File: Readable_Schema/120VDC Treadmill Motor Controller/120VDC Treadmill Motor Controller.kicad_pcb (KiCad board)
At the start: 2 copper layers, 171.2 x 90.5 mm, 75 parts, among them J1 TB005-762-03BE, J2 OSTT7020150, J3 TB0011-350-08BE, J4 TB0011-350-08BE, J5 TB0011-350-08BE, J6 TB0011-350-03BE, J7 TB005-762-02BE, K1 T9GV1L14-24, Q1 IPP200N25N3GXKSA1, Q2 IPP200N25N3GXKSA1, Q4 IPP200N25N3GXKSA1, Q5 MUN5330DW1, Q6 MUN5330DW1T1G, Q7 IPP200N25N3GXKSA1, Q8 SMUN5230DW1T1G, Q9 IPP200N25N3GXKSA1, U1 FOD3182, U10 FOD3182, U11 TC75S56F_LF, U2 FOD3182, U3 TMCS1126B42QDVGRQ1, U4 FOD3182, U5 NLV14044BDR2G, U6 NC7SZ04P5X, U7 FOD3182, U8 RAC05E-05SKT, U9 SN74LVC1G08DCKR

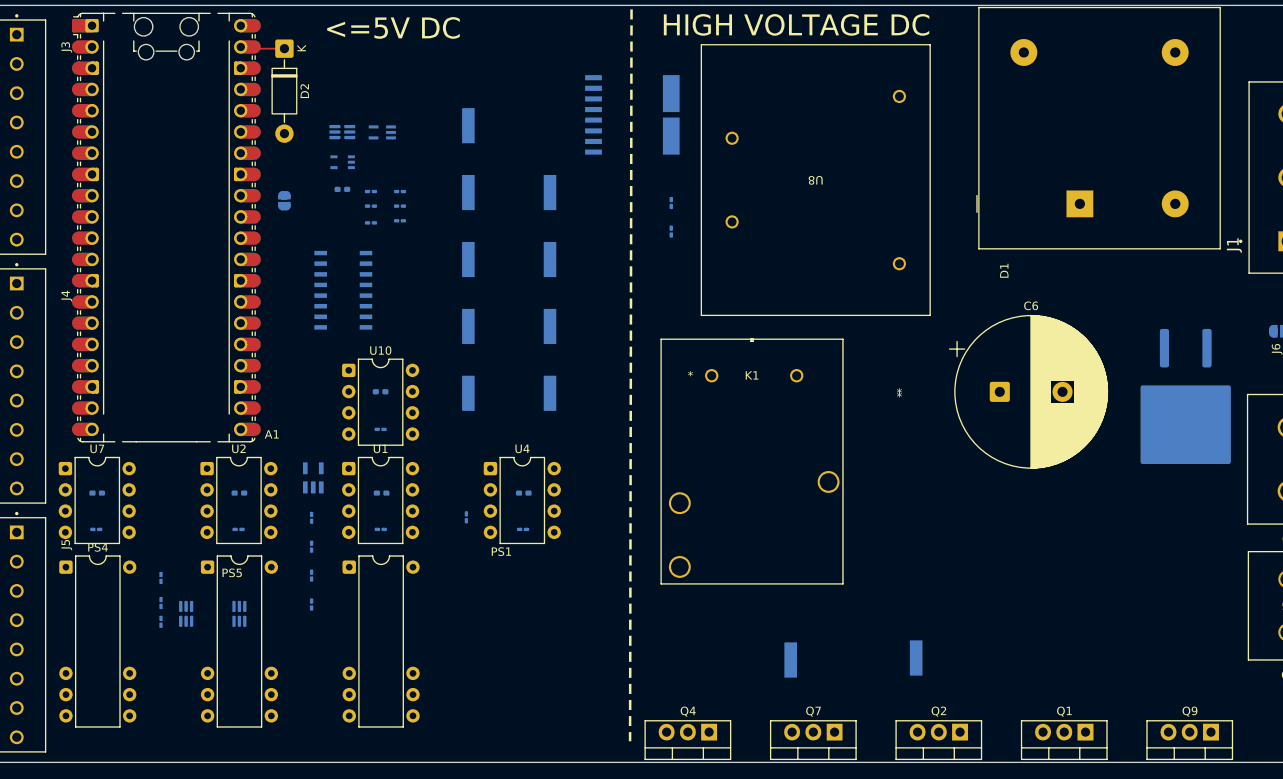
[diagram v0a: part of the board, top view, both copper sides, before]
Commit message: Finished choosing real components for the digitally isolated drives. Mainly followed TIs 100khz example and chose to use mostly repeat components. Now confirming the design doesnt suck then working on traces
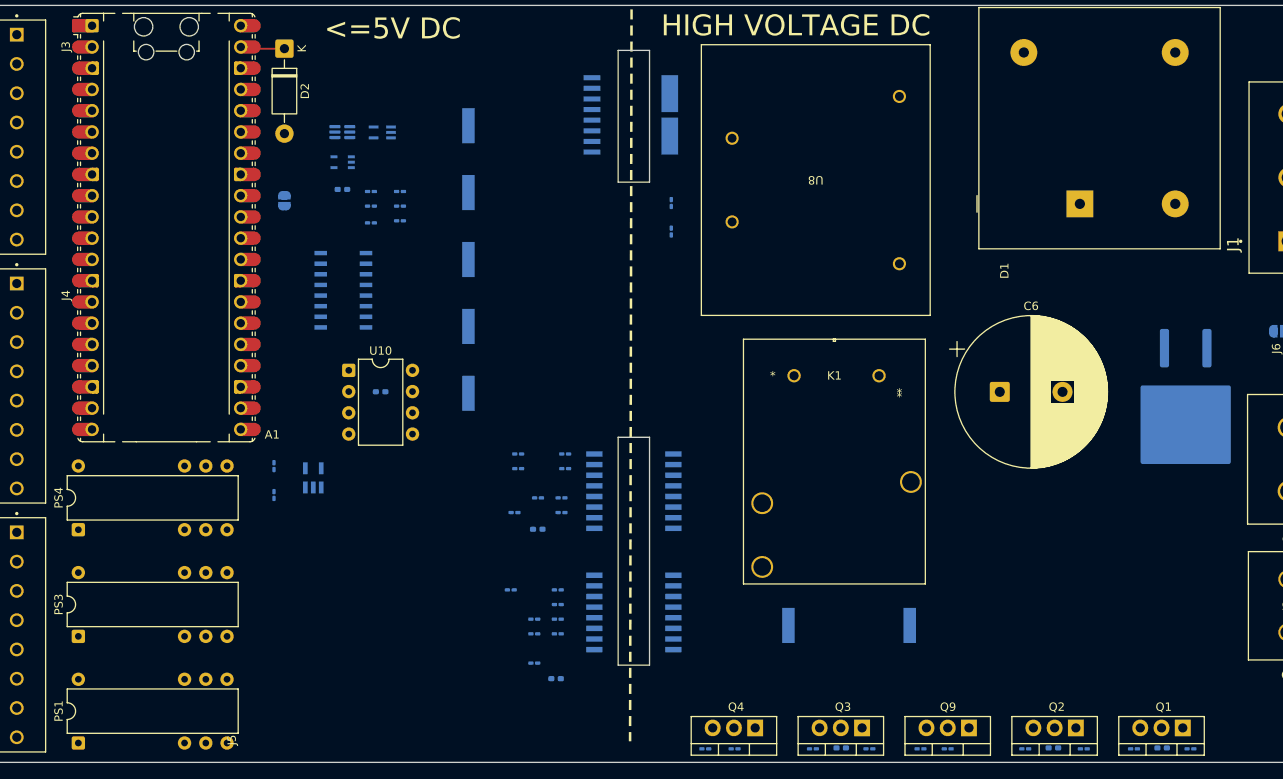
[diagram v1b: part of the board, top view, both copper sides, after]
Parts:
- removed PS5: SRS-0515-2, Footprints_TMC:SRS-0515 DIP-16_W7.62mm
- removed Q6: MUN5330DW1T1G, Package_TO_SOT_SMD:SOT-363_SC-70-6
- removed Q7: IPP200N25N3GXKSA1, Package_TO_SOT_THT:TO-220-3_Vertical
- removed Q8: SMUN5230DW1T1G, Package_TO_SOT_SMD:SOT-363_SC-70-6
- removed TP3, TP4, TP5, TP6: RCWCTE, Treadmill_Feet:RCWCTE
- removed U4, U7: FOD3182, Package_DIP:DIP-8_W7.62mm
- added C10: 0.1u, Capacitor_SMD:C_0402_1005Metric_Pad0.74x0.62mm_HandSolder, B.Cu at (213.2, 148.4)
- added C11: 0.1u, Capacitor_SMD:C_0402_1005Metric_Pad0.74x0.62mm_HandSolder, B.Cu at (200.2, 148.4)
- added C12: 0.1u, Capacitor_SMD:C_0402_1005Metric_Pad0.74x0.62mm_HandSolder, B.Cu at (174.8, 148.4)
- added C13: 33pF, Capacitor_SMD:C_0201_0603Metric_Pad0.64x0.40mm_HandSolder, B.Cu at (141.4, 120.2)
- added C14: 33pF, Capacitor_SMD:C_0201_0603Metric_Pad0.64x0.40mm_HandSolder, B.Cu at (141.8, 113.2)
- added C15: 33pF, Capacitor_SMD:C_0201_0603Metric_Pad0.64x0.40mm_HandSolder, B.Cu at (141.8, 115.0)
- added C16: 0.1u, Capacitor_SMD:C_0402_1005Metric_Pad0.74x0.62mm_HandSolder, B.Cu at (138.5, 122.2)
- added C8: 33pF, Capacitor_SMD:C_0201_0603Metric_Pad0.64x0.40mm_HandSolder, B.Cu at (140.9, 134.8)
- added C9: 33pF, Capacitor_SMD:C_0201_0603Metric_Pad0.64x0.40mm_HandSolder, B.Cu at (141.4, 118.5)
- added PS3: SRS-0515-2, Footprints_TMC:SRS-0515 DIP-16_W7.62mm, F.Cu at (83.6, 135.1)
- added Q3: IPP200N25N3GXKSA1, Package_TO_SOT_THT:TO-220-3_Vertical, F.Cu at (177.3, 146.0)
- added R18: 10K, Resistor_SMD:R_0201_0603Metric_Pad0.64x0.40mm_HandSolder, B.Cu at (136.2, 113.2)
- added R23: 10K, Resistor_SMD:R_0201_0603Metric_Pad0.64x0.40mm_HandSolder, B.Cu at (136.2, 115.0)
- added R24: 10, Resistor_SMD:R_0201_0603Metric_Pad0.64x0.40mm_HandSolder, B.Cu at (209.8, 148.5)
- added R25: 10, Resistor_SMD:R_0201_0603Metric_Pad0.64x0.40mm_HandSolder, B.Cu at (158.6, 148.5)
- added R26: 10K, Resistor_SMD:R_0201_0603Metric_Pad0.64x0.40mm_HandSolder, B.Cu at (216.6, 148.5)
- added R27: 10K, Resistor_SMD:R_0201_0603Metric_Pad0.64x0.40mm_HandSolder, B.Cu at (162.1, 148.5)
- added R28: 10K, Resistor_SMD:R_0201_0603Metric_Pad0.64x0.40mm_HandSolder, B.Cu at (187.5, 148.5)
- C1, C2, C3: value 0.1u -> 33pF; footprint Capacitor_SMD:C_0402_1005Metric_Pad0.74x0.62mm_HandSolder -> Capacitor_SMD:C_0201_0603Metric_Pad0.64x0.40mm_HandSolder
- R1, R2: value 10 -> 50
- R10, R5: value 100 -> 10K
- R15, R6: value 10 -> 10K
- R16, R4: value 100 -> 50
- R7, R8: value 100 -> 10
- U1, U2: value FOD3182 -> UCC21530DWKR; footprint Package_DIP:DIP-8_W7.62mm -> Treadmill_Feet:SOIC127P1030X265-16N; moved to B.Cu
- moved R7 105.3 mm to (196.8, 148.5), turned to 0 degrees
- moved R15 96.1 mm to (178.2, 148.5), turned to 0 degrees
- moved R10 95.4 mm to (203.8, 148.5), turned to 0 degrees
- moved R8 79.9 mm to (171.4, 148.5), turned to 0 degrees
- moved R12 75.0 mm to (184.3, 148.5), turned to 0 degrees
- moved C5 59.2 mm to (140.7, 140.1)
- moved U2 53.8 mm to (150.0, 132.2)
- moved R5 44.9 mm to (138.1, 138.2), turned to 180 degrees
- moved C2 40.3 mm to (140.9, 131.2)
- moved PS1 38.6 mm to (83.6, 147.8), turned to 90 degrees
- moved R2 37.5 mm to (138.1, 134.8)
- moved U1 34.2 mm to (150.0, 117.7)
- moved Q9 28.9 mm to (190.1, 146.0)
- moved R4 27.2 mm to (138.6, 118.5), turned to 180 degrees
- moved C1 24.0 mm to (140.9, 129.5)
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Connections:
- A1 pad 27: /H_Bridge/dir -> /Pi Pico/dir_mcu
- C1 pad 1: GND1 -> Net-(U2-INB)
- C1 pad 2: /Brake_Resistor/ps_in_+ -> GND
- C2 pad 1: /H_Bridge/Fet Circuit1/lg -> Net-(U2-DT)
- C2 pad 2: Net-(U2-VCC) -> GND
- C3 pad 1: GND1 -> Net-(U2-INA)
- C3 pad 2: /Brake_Resistor/ps_in_+ -> GND
- C5 pad 1: /H_Bridge/Fet Circuit/lg -> 5v 5w
- C5 pad 2: Net-(U7-VCC) -> GND
- J2 pad 1: /H_Bridge/Fet Circuit/lg -> /H_Bridge/hs_ps_1_-
- J2 pad 2: /H_Bridge/Fet Circuit1/lg -> /H_Bridge/hs_ps_2_-
- PS1 pad 7: /Brake_Resistor/ps_in_+ -> /H_Bridge/ls_ps_+
- PS4 pad 11: /H_Bridge/Fet Circuit/lg -> /H_Bridge/hs_ps_2_-
- PS4 pad 7: Net-(U7-VCC) -> /H_Bridge/hs_ps_2_+
- Q1 pad 1: /H_Bridge/Fet Circuit/lg -> /Feedback/in-
- Q1 pad 3: GND1 -> /H_Bridge/hs_ps_2_-
- Q2 pad 3: /H_Bridge/Fet Circuit1/lg -> /H_Bridge/hs_ps_1_-
- Q4 pad 1: /H_Bridge/Fet Circuit1/lg -> /H_Bridge/hs_ps_2_-
- R1 pad 1: Net-(R1-Pad1) -> /H_Bridge/dir_b
- R1 pad 2: Net-(Q1-G) -> Net-(U2-INB)
- R10 pad 1: 3v3 MCU -> /H_Bridge/hs_ps_1_-
- R10 pad 2: Net-(Q8B-C2) -> Net-(Q2-G)
- R15 pad 1: Net-(R15-Pad1) -> GND1
- R15 pad 2: Net-(Q7-G) -> Net-(Q3-G)
- R16 pad 1: /H_Bridge/LS FET/v_pwm -> /H_Bridge/dir_a
- R16 pad 2: /H_Bridge/dir -> Net-(U1-INB)
- R2 pad 1: Net-(R2-Pad1) -> /H_Bridge/pwm_a
- R2 pad 2: Net-(Q2-G) -> Net-(U2-INA)
- R4 pad 1: Net-(Q8B-C2) -> /H_Bridge/pwm_b
- R4 pad 2: /H_Bridge/LS FET1/v_pwm -> Net-(U1-INA)
- R5 pad 1: Net-(Q6B-C2) -> Net-(U2-EN)
- R5 pad 2: /H_Bridge/Fet Circuit/v_pwm -> Net-(U2-VCCI_2)
- R6 pad 1: Net-(R6-Pad1) -> Net-(U2-DT)
- R6 pad 2: Net-(Q4-G) -> GND
- R7 pad 1: /H_Bridge/Fet Circuit1/v_pwm -> Net-(U2-OUTA)
- R7 pad 2: Net-(Q8A-C1) -> Net-(Q2-G)
- R8 pad 1: Net-(Q8A-C1) -> Net-(U2-OUTB)
- R8 pad 2: /Feedback/pwm -> Net-(Q3-G)
- TP1 pad 1: /H_Bridge/Fet Circuit/lg -> /H_Bridge/hs_ps_1_-
- TP2 pad 1: /H_Bridge/Fet Circuit1/lg -> /H_Bridge/hs_ps_2_-
- U1 pad 1: unconnected-(U1-NC-Pad1) -> Net-(U1-INA)
- U1 pad 2: GND1 -> Net-(U1-INB)
- U1 pad 3: /H_Bridge/LS FET1/v_pwm -> 5v 5w
- U1 pad 4: unconnected-(U1-NC-Pad4) -> GND
- U1 pad 5: GND1 -> Net-(U1-EN)
- U1 pad 6: Net-(R1-Pad1) -> Net-(U1-DT)
- U1 pad 7: Net-(R1-Pad1) -> unconnected-(U1-NC-Pad7)
- U1 pad 8: /Brake_Resistor/ps_in_+ -> Net-(U1-VCCI_2)
- U2 pad 1: unconnected-(U2-NC-Pad1) -> Net-(U2-INA)
- U2 pad 2: GND -> Net-(U2-INB)
- U2 pad 3: /H_Bridge/Fet Circuit1/v_pwm -> 5v 5w
- U2 pad 4: unconnected-(U2-NC-Pad4) -> GND
- U2 pad 5: /H_Bridge/Fet Circuit1/lg -> Net-(U2-EN)
- U2 pad 6: Net-(R2-Pad1) -> Net-(U2-DT)
- U2 pad 7: Net-(R2-Pad1) -> unconnected-(U2-NC-Pad7)
- U2 pad 8: Net-(U2-VCC) -> Net-(U2-VCCI_2)
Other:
- outline, holes or cut-outs redrawn

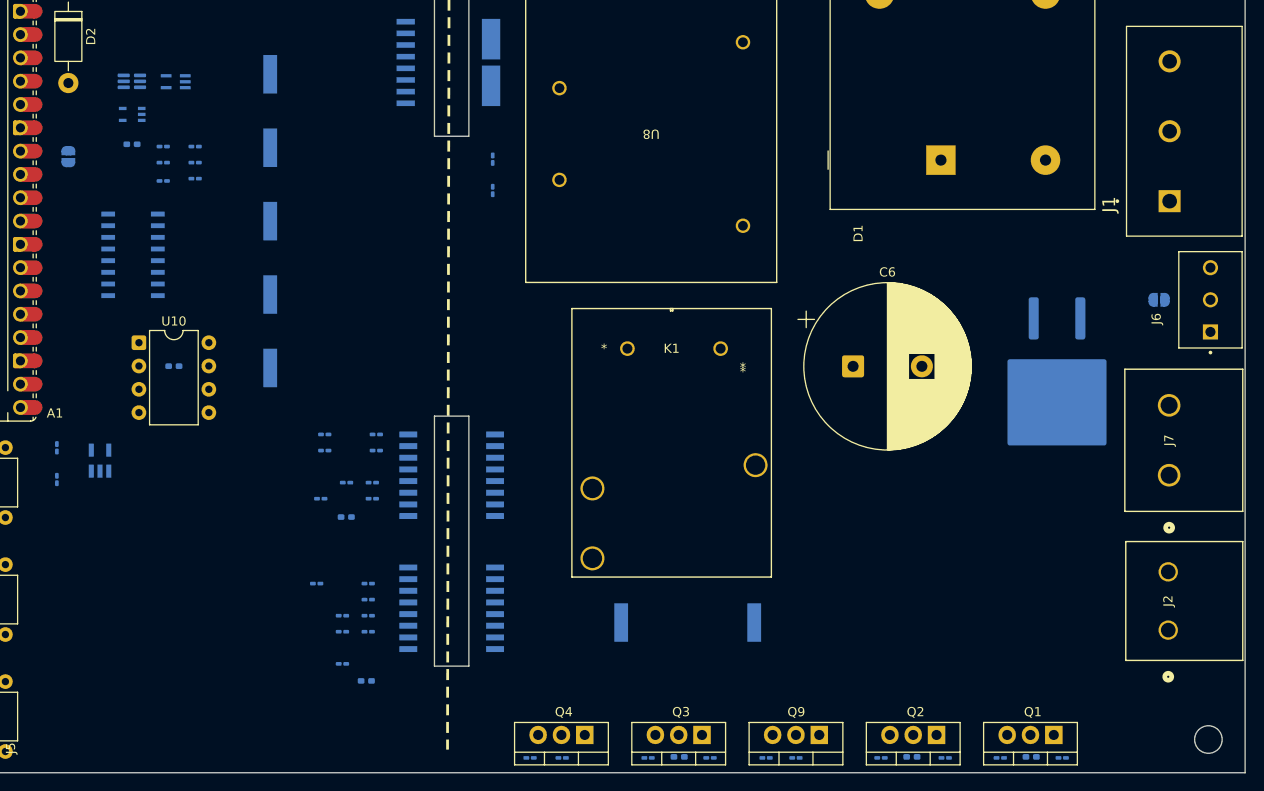
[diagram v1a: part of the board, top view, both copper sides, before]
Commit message: -Removed brake resistor subcircuit -Worked up bus cap to 4x 820uF 400V caps -changed the fets to 600V 49A 60mOhm RdsON --------------------------------------------- -need different isolated power supplies --May want to consider a bootstrap circuit since we wont be needing 100% duty cycle -need to resize gate resistors -Need to change out bridge rectifier to be vertical for ease of mounting heatsink
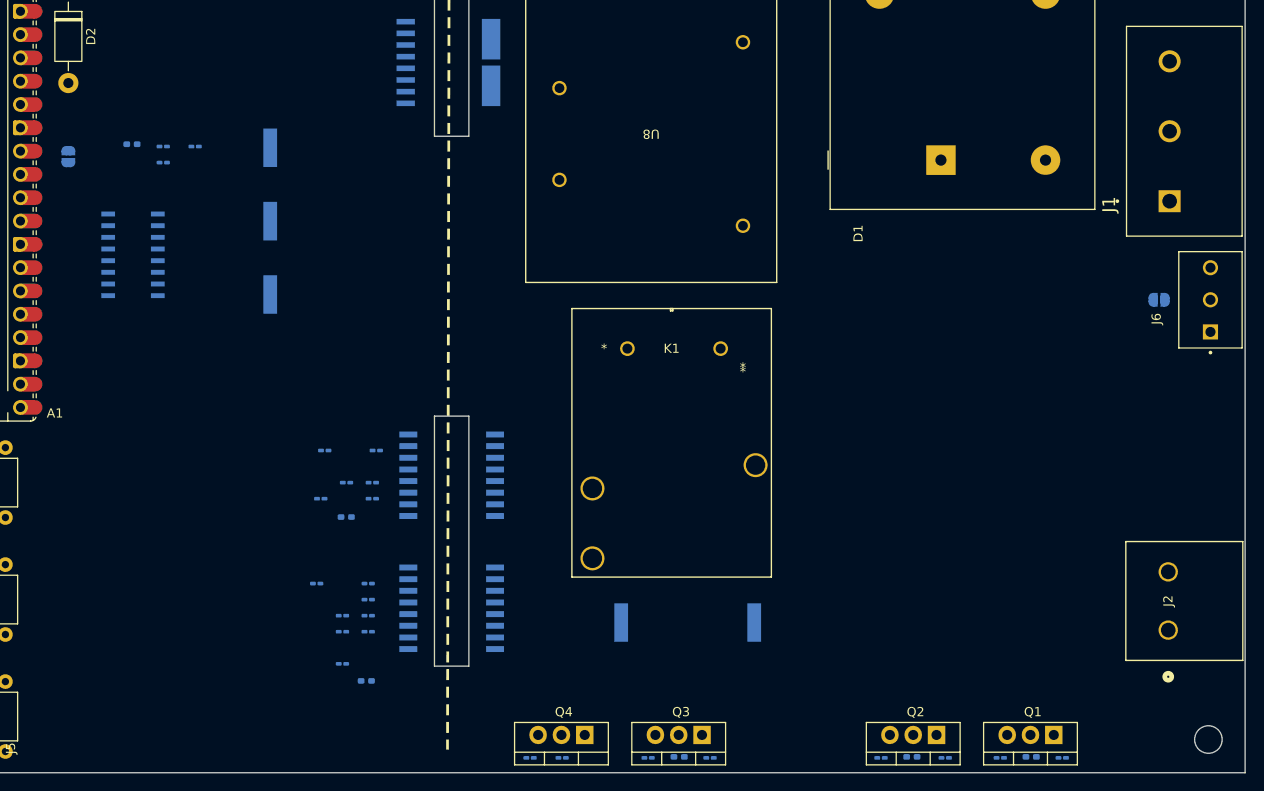
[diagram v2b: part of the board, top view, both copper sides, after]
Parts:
- removed C14: 33pF, Capacitor_SMD:C_0201_0603Metric_Pad0.64x0.40mm_HandSolder
- removed C6: 200uF, Capacitor_THT:CP_Radial_D18.0mm_P7.50mm
- removed C7: 0.1u, Capacitor_SMD:C_0402_1005Metric_Pad0.74x0.62mm_HandSolder
- removed D4: STTH30L06G-TR, Package_TO_SOT_SMD:TO-263-2
- removed J7: TB005-762-02BE, Treadmill_Feet:TB005-762-02BE_CUD
- removed Q5: MUN5330DW1, Package_TO_SOT_SMD:SOT-363_SC-70-6
- removed Q9: IPP200N25N3GXKSA1, Package_TO_SOT_THT:TO-220-3_Vertical
- removed R11: 10M, Resistor_SMD:R_0201_0603Metric_Pad0.64x0.40mm_HandSolder
- removed R12: 10, Resistor_SMD:R_0201_0603Metric_Pad0.64x0.40mm_HandSolder
- removed R17: 1K, Resistor_SMD:R_0201_0603Metric_Pad0.64x0.40mm_HandSolder
- removed R18, R21, R28: 10K, Resistor_SMD:R_0201_0603Metric_Pad0.64x0.40mm_HandSolder
- removed R19: 1.2Meg, Resistor_SMD:R_0201_0603Metric_Pad0.64x0.40mm_HandSolder
- removed R20: 9K, Resistor_SMD:R_0201_0603Metric_Pad0.64x0.40mm_HandSolder
- removed R22: 8.2K, Resistor_SMD:R_0201_0603Metric_Pad0.64x0.40mm_HandSolder
- removed R9: 16K, Resistor_SMD:R_0201_0603Metric_Pad0.64x0.40mm_HandSolder
- removed TP11, TP7: RCWCTE, Treadmill_Feet:RCWCTE
- removed U10: FOD3182, Package_DIP:DIP-8_W7.62mm
- removed U11: TC75S56F_LF, Treadmill_Feet:SOT-25 SMV_TOS
- removed U6: NC7SZ04P5X, Treadmill_Feet:SC-88A-5_1P35X2P2_ONS
- removed U9: SN74LVC1G08DCKR, Treadmill_Feet:DCK5
- R13, R3: value 10M -> 5K
- R5: value 10K -> 5K
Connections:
- net GND renamed LV_GND
- net Net-(U5-*R0) renamed /Feedback/Reset
- A1 pad 21: unconnected-(A1-GPIO16-Pad21) -> /H_Bridge/dir_b
- A1 pad 22: unconnected-(A1-GPIO17-Pad22) -> /H_Bridge/pwm_b
- A1 pad 27: /Pi Pico/dir_mcu -> /H_Bridge/dir_a
- A1 pad 29: /Feedback/pwm -> /H_Bridge/pwm_a
- C12 pad 2: GND1 -> HV_GND
- C8 pad 1: Net-(U2-EN) -> /H_Bridge/EN_drive
- D1 pad 3: GND1 -> HV_GND
- PS1 pad 11: GND1 -> HV_GND
- Q1 pad 1: /Feedback/in- -> 170V Rect
- Q2 pad 1: /Feedback/in- -> 170V Rect
- Q3 pad 3: GND1 -> /Feedback/in+
- Q4 pad 3: GND1 -> /Feedback/in+
- R15 pad 1: GND1 -> /Feedback/in+
- R27 pad 1: GND1 -> /Feedback/in+
- R5 pad 1: Net-(U2-EN) -> /Feedback/EN_Drives
- R5 pad 2: Net-(U2-VCCI_2) -> /H_Bridge/EN_drive
- U1 pad 5: Net-(U1-EN) -> /H_Bridge/EN_drive
- U1 pad 8: Net-(U1-VCCI_2) -> unconnected-(U1-VCCI_2-Pad8)
- U1 pad 9: GND1 -> /Feedback/in+
- U2 pad 5: Net-(U2-EN) -> /H_Bridge/EN_drive
- U2 pad 8: Net-(U2-VCCI_2) -> unconnected-(U2-VCCI_2-Pad8)
- U2 pad 9: GND1 -> /Feedback/in+
- U3 pad 1: 170V Rect -> /Feedback/in+
- U3 pad 2: /Feedback/in- -> HV_GND
- U3 pad 3: Net-(Q5B-B2) -> /Feedback/OC_out
- U5 pad 13: /Feedback/SR_out -> /Feedback/EN_Drives
- U5 pad 16: 3v3 MCU -> 5v 5w
- U5 pad 5: 3v3 MCU -> /Feedback/OC_out
